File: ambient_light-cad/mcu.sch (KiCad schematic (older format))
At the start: 30 parts

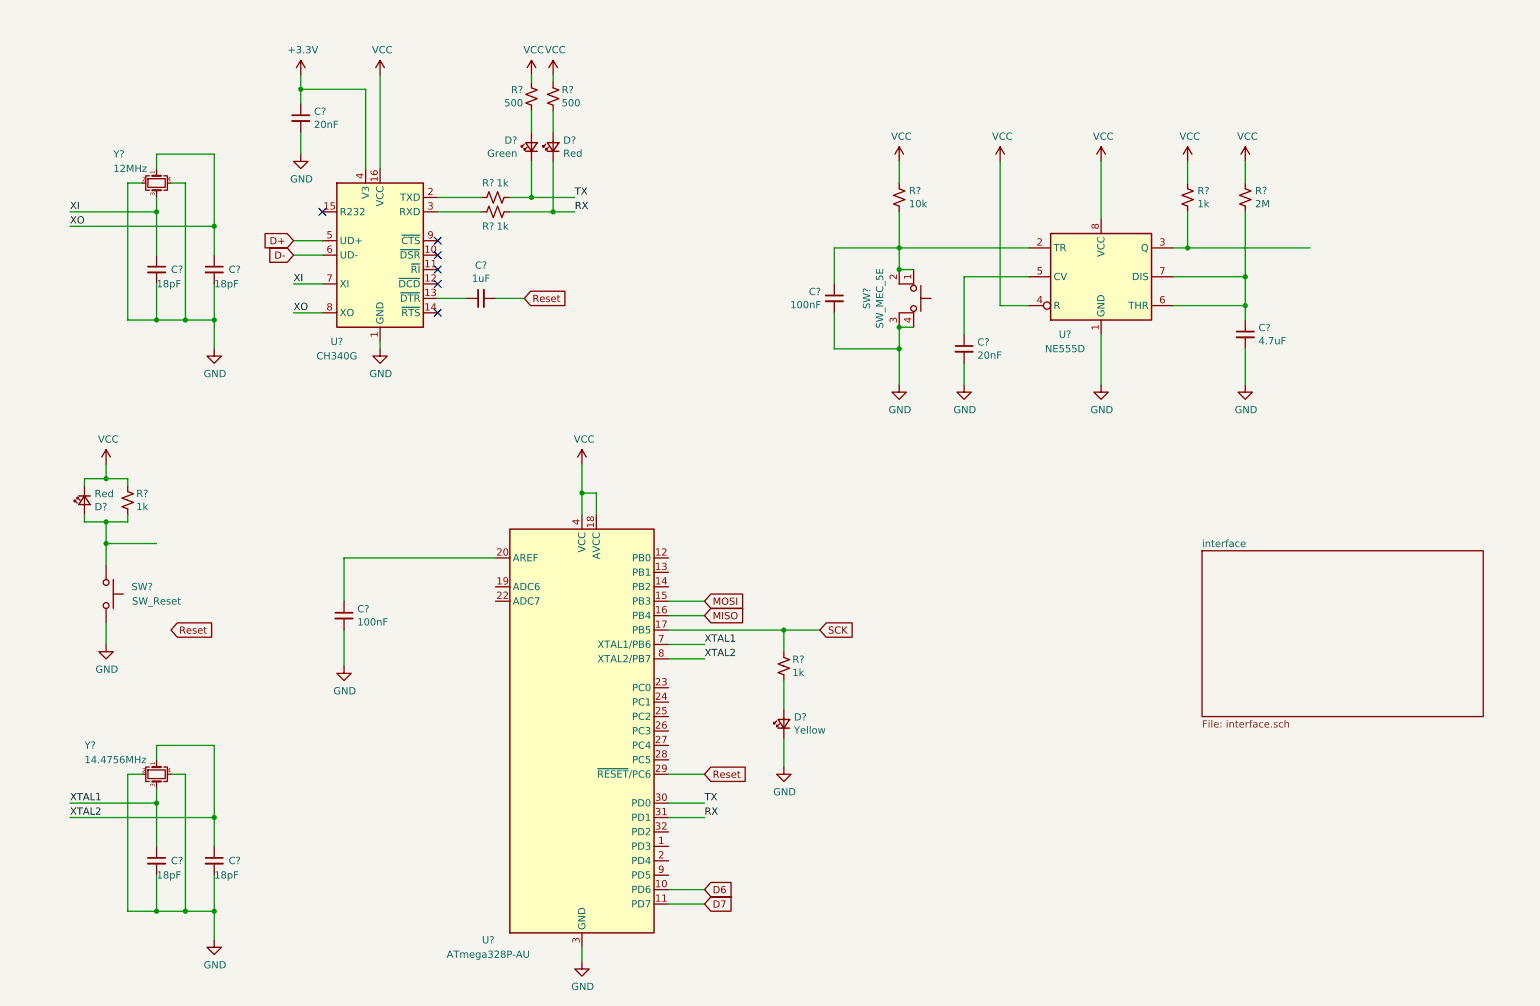
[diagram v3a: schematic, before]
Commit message: [Added] NE555 ouput OP amp
RST_Trigger signal을 OP amp와 MOSFET 과 연결
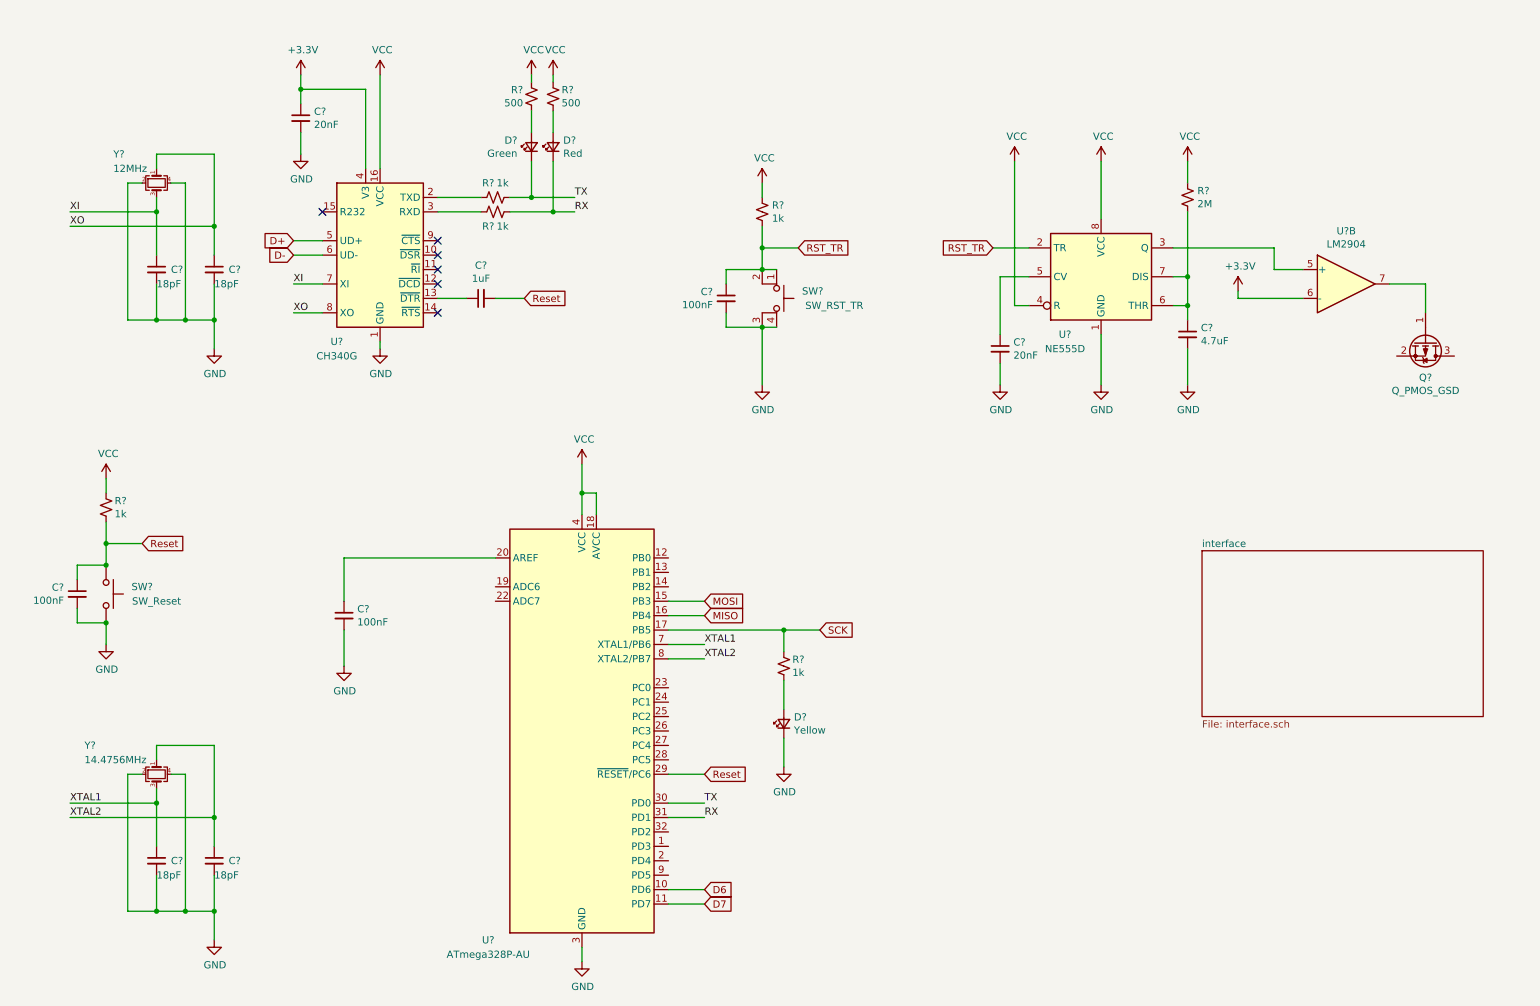
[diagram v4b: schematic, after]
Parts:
- removed D?: Red, symbol Device:LED_Small
- removed R?: 1k, symbol Device:R_Small_US
- added C?: 100nF, symbol Device:C_Small
- added Q?: Q_PMOS_GSD, symbol Device:Q_PMOS_GSD
- added U?: LM2904, symbol Amplifier_Operational:LM2904
- R?: value 10k -> 1k
- SW?: value SW_MEC_5E -> SW_RST_TR
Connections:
- net +3V3: now also U?.6 (-)
- net GND: now also C?.2
- net Reset: now also R?.2, SW?.1, C?.1
- net RST_TR: now reaches C?.1, R?.2, SW?.1, SW?.2, U?.2 (TR)
- net at U?.3 (Q): now also U?.5 (+)
- new net: Q?.1 (G), U?.7
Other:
- moved on the sheet: C?, R?, SW?

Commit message: [Added] MOSFET wiring
Wiring MOSFET
Changed OP-AMP
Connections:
- net +3V3: now also U?.5 (+); no longer U?.6 (-)
- net Reset: now also Q?.3 (D); no longer C?.2
- net at U?.3 (Q): now also U?.6 (-); no longer U?.5 (+)
- net RST_MOS: now reaches Q?.2 (S)
- net RST_MOS: now also C?.2
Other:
- moved on the sheet: Q?, U?B
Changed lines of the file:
@@
 Text GLabel 5350 6000 2    50   Input ~ 0
-Reset
-Text GLabel 4100 2700 2    50   Input ~ 0
 Reset
 Connection ~ 5900 5000
@@
 	1    0    0    -1
 $EndComp
-Wire Wire Line
-	3900 2700 4100 2700
 $Comp
 L Device:R_Small_US R?
@@
 L power:+3.3V #PWR?
 U 1 1 5FDC074A
-P 9050 2650
-F 0 "#PWR?" H 9050 2500 50  0001 C CNN
-F 1 "+3.3V" H 9065 2823 50  0000 C CNN
-F 2 "" H 9050 2650 50  0001 C CNN
-F 3 "" H 9050 2650 50  0001 C CNN
-	1    9050 2650
-	1    0    0    -1
-$EndComp
-Wire Wire Line
-	9050 2650 9050 2700
-Wire Wire Line
-	9050 2700 9500 2700
-Wire Wire Line
-	9300 2350 9300 2500
-Wire Wire Line
-	9300 2500 9500 2500
+P 9150 1750
+F 0 "#PWR?" H 9150 1600 50  0001 C CNN
+F 1 "+3.3V" H 9165 1923 50  0000 C CNN
+F 2 "" H 9150 1750 50  0001 C CNN
+F 3 "" H 9150 1750 50  0001 C CNN
+	1    9150 1750
+	1    0    0    -1
+$EndComp
 Wire Wire Line
 	7500 2750 7600 2750
@@
 L Amplifier_Operational:LM2904 U?
 U 2 1 5FF329A5
-P 9800 2600
-F 0 "U?" H 9800 2967 50  0000 C CNN
-F 1 "LM2904" H 9800 2876 50  0000 C CNN
-F 2 "" H 9800 2600 50  0001 C CNN
-F 3 "http://www.ti.com/lit/ds/symlink/lm358.pdf" H 9800 2600 50  0001 C CNN
-	2    9800 2600
-	1    0    0    -1
-$EndComp
-Wire Wire Line
-	8600 2350 9300 2350
+P 9800 2250
+F 0 "U?" H 9800 2617 50  0000 C CNN
+F 1 "LM2904" H 9800 2526 50  0000 C CNN
+F 2 "" H 9800 2250 50  0001 C CNN
+F 3 "http://www.ti.com/lit/ds/symlink/lm358.pdf" H 9800 2250 50  0001 C CNN
+	2    9800 2250
+	1    0    0    -1
+$EndComp
 $Comp
 L Device:Q_PMOS_GSD Q?
 U 1 1 5FF3F91D
-P 10350 3000
-F 0 "Q?" V 10599 3000 50  0000 C CNN
-F 1 "Q_PMOS_GSD" V 10690 3000 50  0000 C CNN
-F 2 "" H 10550 3100 50  0001 C CNN
-F 3 "~" H 10350 3000 50  0001 C CNN
-	1    10350 3000
+P 10350 2650
+F 0 "Q?" V 10599 2650 50  0000 C CNN
+F 1 "Q_PMOS_GSD" V 10690 2650 50  0000 C CNN
+F 2 "" H 10550 2750 50  0001 C CNN
+F 3 "~" H 10350 2650 50  0001 C CNN
+	1    10350 2650
 	0    1    1    0
 $EndComp
 Wire Wire Line
-	10100 2600 10350 2600
-Wire Wire Line
-	10350 2600 10350 2800
+	10100 2250 10350 2250
+Wire Wire Line
+	10350 2250 10350 2450
+Wire Wire Line
+	8600 2350 9500 2350
+Wire Wire Line
+	9500 2150 9150 2150
+Wire Wire Line
+	9150 1750 9150 2150
+Text GLabel 10700 2750 2    50   Input ~ 0
+Reset
+Wire Wire Line
+	10150 2750 10000 2750
+Wire Wire Line
+	10550 2750 10700 2750
+Text GLabel 4100 2700 2    50   Input ~ 0
+RST_MOS
+Text GLabel 10000 2750 0    50   Input ~ 0
+RST_MOS
+Wire Wire Line
+	3900 2700 4100 2700
 $EndSCHEMATC

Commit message: [Added] Slide SW for Reset Trigger
단가 절감을 위해 슬라이드 스위치 방식 추가
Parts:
- added R?: 1k, symbol Device:R_Small_US
- added SW?: SW_SPDT, symbol Switch:SW_SPDT
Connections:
- net GND: now also R?.2
- net RST_MOS: now also SW?.2 (B); no longer Q?.2 (S)
- net Reset: now also SW?.1 (A); no longer Q?.3 (D)
- net D5: now reaches U?.9 (PD5)
- net D5: now also R?.1, SW?.3 (C)
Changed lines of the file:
@@
 Wire Wire Line
 	9150 1750 9150 2150
-Text GLabel 10700 2750 2    50   Input ~ 0
+Text GLabel 7450 4050 2    50   Input ~ 0
 Reset
 Wire Wire Line
@@
 Text GLabel 4100 2700 2    50   Input ~ 0
 RST_MOS
-Text GLabel 10000 2750 0    50   Input ~ 0
+Text GLabel 6750 4150 0    50   Input ~ 0
 RST_MOS
 Wire Wire Line
 	3900 2700 4100 2700
+$Comp
+L Switch:SW_SPDT SW?
+U 1 1 5FD8F28F
+P 7100 4150
+F 0 "SW?" H 7100 4435 50  0000 C CNN
+F 1 "SW_SPDT" H 7100 4344 50  0000 C CNN
+F 2 "" H 7100 4150 50  0001 C CNN
+F 3 "~" H 7100 4150 50  0001 C CNN
+	1    7100 4150
+	1    0    0    -1
+$EndComp
+Wire Wire Line
+	6750 4150 6900 4150
+Text GLabel 5350 6700 2    50   Input ~ 0
+D5
+Wire Wire Line
+	5100 6700 5350 6700
+Text GLabel 7600 4250 2    50   Input ~ 0
+D5
+Wire Wire Line
+	7450 4050 7300 4050
+Wire Wire Line
+	7300 4250 7450 4250
+$Comp
+L Device:R_Small_US R?
+U 1 1 5FDB538A
+P 7450 4450
+AR Path="/5FDB538A" Ref="R?"  Part="1"
+AR Path="/5FD145BE/5FDB538A" Ref="R?"  Part="1"
+F 0 "R?" H 7509 4496 50  0000 L CNN
+F 1 "1k" H 7509 4405 50  0000 L CNN
+F 2 "" H 7450 4450 50  0001 C CNN
+F 3 "~" H 7450 4450 50  0001 C CNN
+	1    7450 4450
+	1    0    0    -1
+$EndComp
+Wire Wire Line
+	7450 4350 7450 4250
+Connection ~ 7450 4250
+Wire Wire Line
+	7450 4250 7600 4250
+$Comp
+L power:GND #PWR?
+U 1 1 5FDBE2D5
+P 7450 4650
+AR Path="/5FDBE2D5" Ref="#PWR?"  Part="1"
+AR Path="/5FD145BE/5FDBE2D5" Ref="#PWR?"  Part="1"
+F 0 "#PWR?" H 7450 4400 50  0001 C CNN
+F 1 "GND" H 7455 4477 50  0000 C CNN
+F 2 "" H 7450 4650 50  0001 C CNN
+F 3 "" H 7450 4650 50  0001 C CNN
+	1    7450 4650
+	1    0    0    -1
+$EndComp
+Wire Wire Line
+	7450 4650 7450 4550
 $EndSCHEMATC

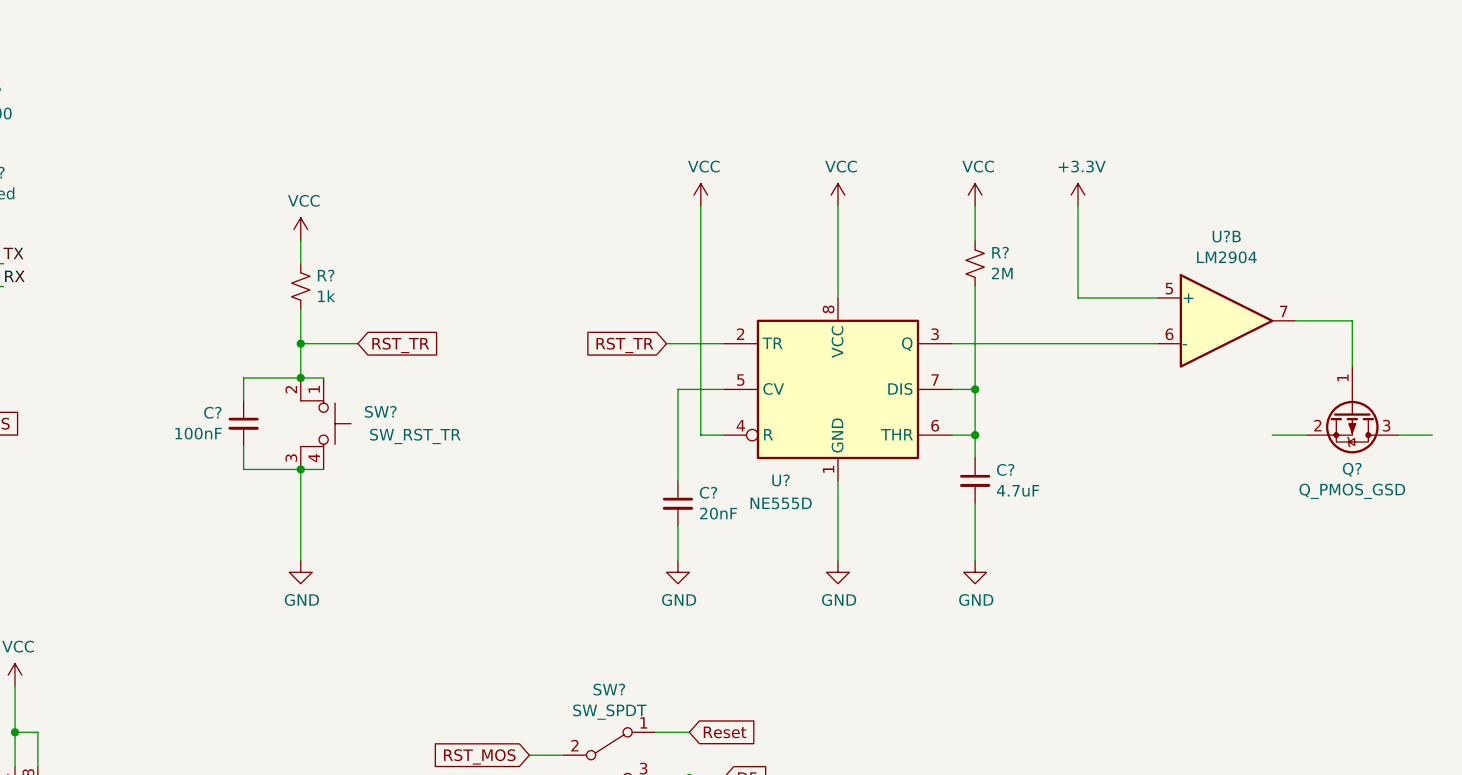
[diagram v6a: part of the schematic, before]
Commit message: [Deleted] NE555 monostable multivibrator
Reset pin trigger 를 위해 구성한 NE555 로직 및 Op amp 제거
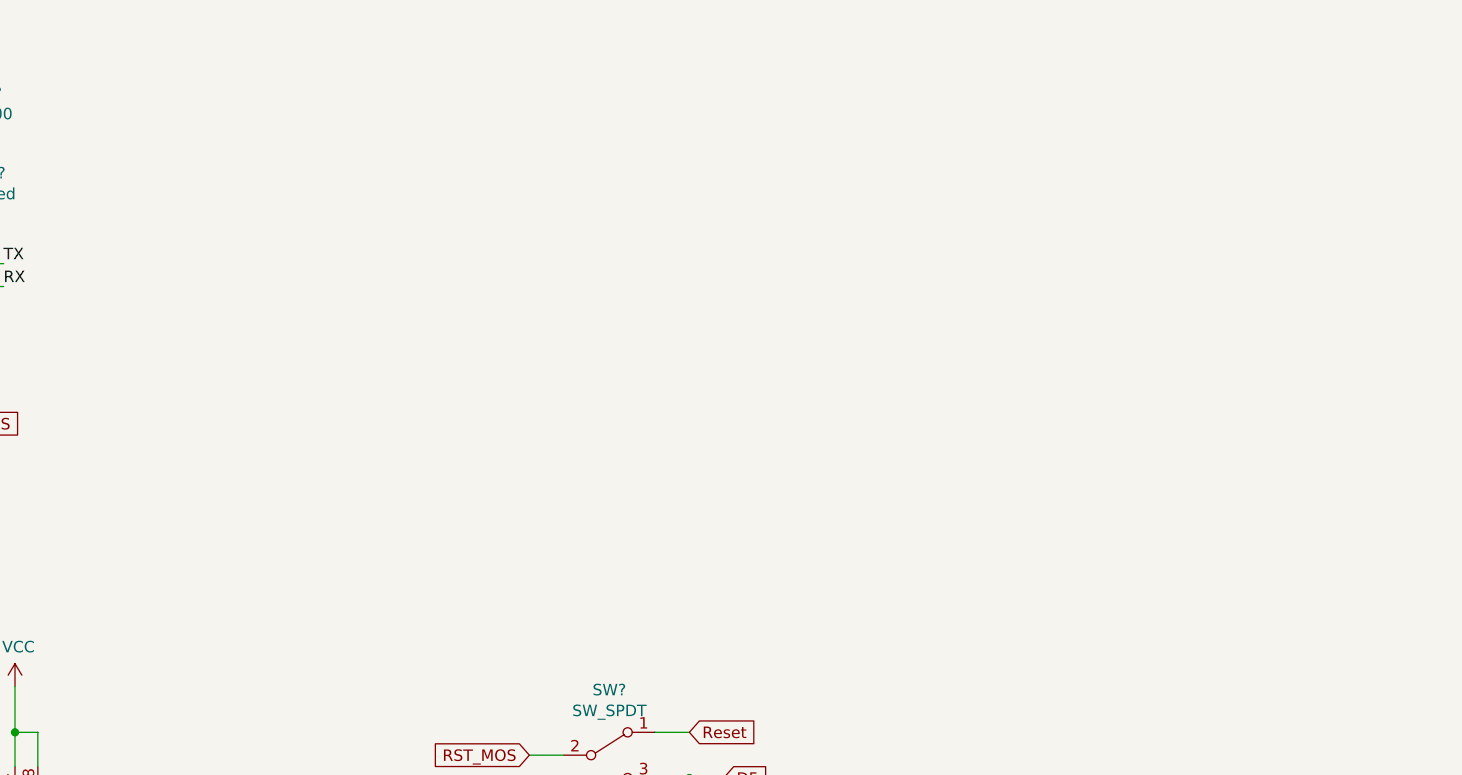
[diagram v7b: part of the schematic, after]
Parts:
- removed C?: 20nF, symbol Device:C_Small
- removed C?: 4.7uF, symbol Device:C_Small
- removed C?: 100nF, symbol Device:C_Small
- removed Q?: Q_PMOS_GSD, symbol Device:Q_PMOS_GSD
- removed R?: 1k, symbol Device:R_Small_US
- removed R?: 2M, symbol Device:R_Small_US
- removed SW?: SW_RST_TR, symbol Switch:SW_MEC_5E
- removed U?: NE555D, Package_SO:SOIC-8_3.9x4.9mm_P1.27mm, symbol Timer:NE555D
- removed U?: LM2904, symbol Amplifier_Operational:LM2904
